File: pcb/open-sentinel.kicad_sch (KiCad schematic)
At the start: 0 parts

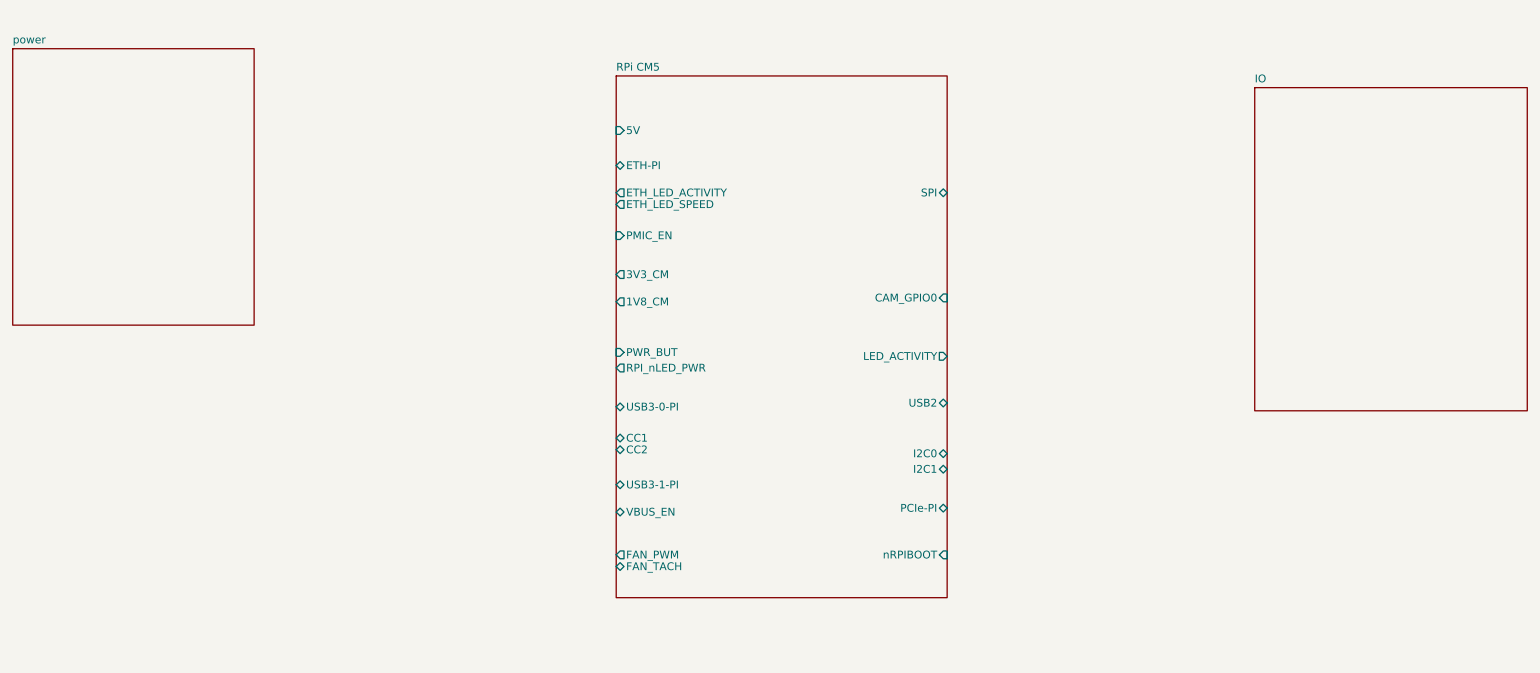
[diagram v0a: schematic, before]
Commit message: add HDMI and CSI pages
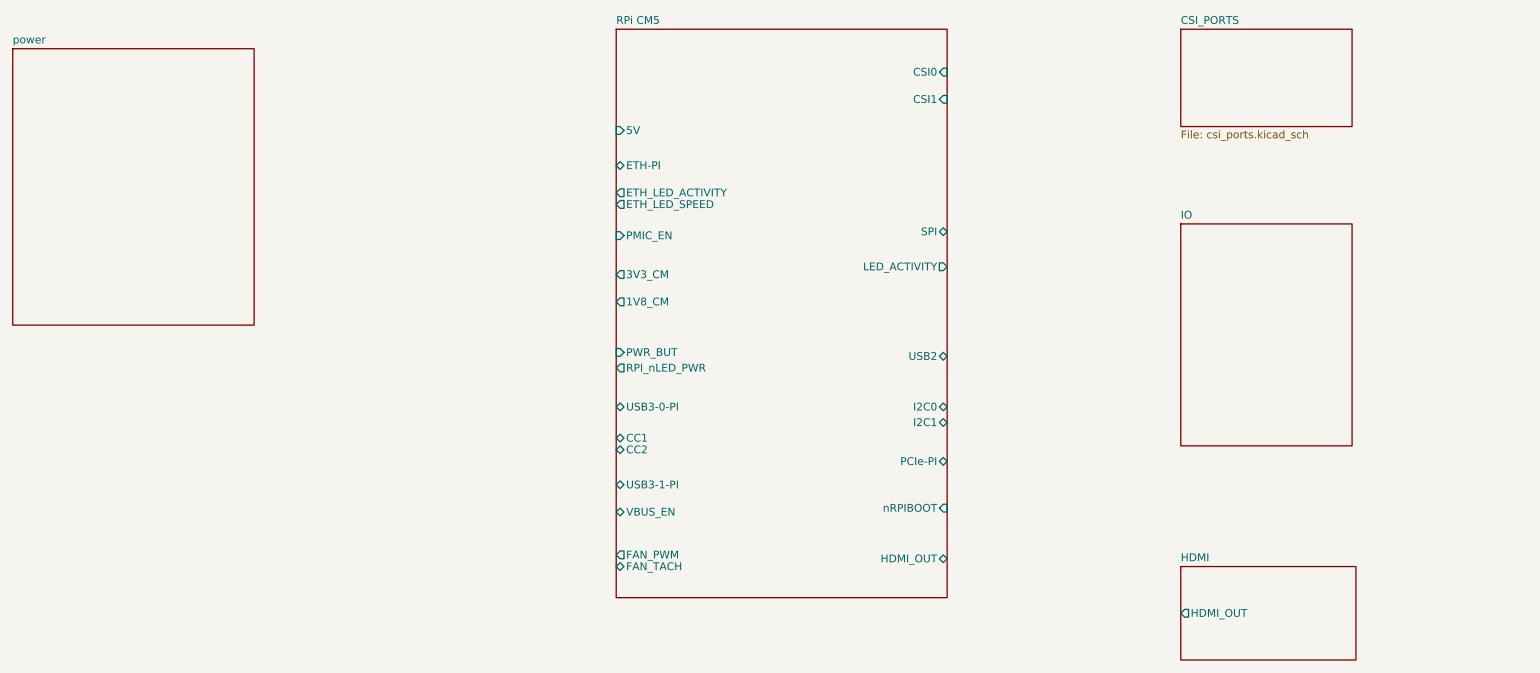
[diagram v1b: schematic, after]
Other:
- added sheet CSI_PORTS (csi_ports.kicad_sch)
- added sheet HDMI (hdmi.kicad_sch)
- sheet RPi CM5 ports: added CSI0, CSI1, HDMI_OUT; removed CAM_GPIO0
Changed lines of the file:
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@@
 	)
 	(sheet
-		(at 273.05 98.425)
-		(size 44.45 52.705)
+		(at 260.985 88.9)
+		(size 27.94 15.875)
+		(exclude_from_sim no)
+		(in_bom yes)
+		(on_board yes)
+		(dnp no)
+		(fields_autoplaced yes)
+		(stroke
+			(width 0.1524)
+			(type solid)
+			(color 132 0 0 1)
+		)
+		(fill
+			(color 255 255 194 1.0000)
+		)
+		(property "Sheetname" "CSI_PORTS"
+			(at 260.985 88.1884 0)
+			(effects
+				(font
+					(size 1.27 1.27)
+				)
+				(justify left bottom)
+			)
+		)
+		(property "Sheetfile" "csi_ports.kicad_sch"
+			(at 260.985 105.3596 0)
+			(effects
+				(font
+					(size 1.27 1.27)
+				)
+				(justify left top)
+			)
+		)
+		(instances
+			(project "open-sentinel"
+				(path "/b7d228cf-f9da-4203-b1ed-1128e1073415"
+					(page "6")
+				)
+			)
+		)
+	)
+	(sheet
+		(at 260.985 176.53)
+		(size 28.575 15.24)
 		(exclude_from_sim no)
 		(in_bom yes)
@@
 			(color 255 255 194 1.0000)
 		)
-		(property "Sheetname" "IO"
-			(at 273.05 97.7134 0)
+		(property "Sheetname" "HDMI"
+			(at 260.985 175.8184 0)
 			(effects
 				(font
@@
 			)
 		)
-		(property "Sheetfile" "io.kicad_sch"
-			(at 273.05 151.7146 0)
+		(property "Sheetfile" "hdmi.kicad_sch"
+			(at 260.985 192.3546 0)
 			(effects
 				(font
@@
 				(justify left top)
 				(hide yes)
+			)
+		)
+		(pin "HDMI_OUT" output
+			(at 260.985 184.15 180)
+			(effects
+				(font
+					(size 1.27 1.27)
+				)
+				(justify left)
 			)
 		)
@@
 			(project "open-sentinel"
 				(path "/b7d228cf-f9da-4203-b1ed-1128e1073415"
-					(page "4")
+					(page "5")
 				)
 			)
@@
 	)
 	(sheet
-		(at 168.91 96.52)
-		(size 53.975 85.09)
+		(at 260.985 120.65)
+		(size 27.94 36.195)
 		(exclude_from_sim no)
 		(in_bom yes)
@@
 			(color 255 255 194 1.0000)
 		)
+		(property "Sheetname" "IO"
+			(at 260.985 119.9384 0)
+			(effects
+				(font
+					(size 1.27 1.27)
+				)
+				(justify left bottom)
+			)
+		)
+		(property "Sheetfile" "io.kicad_sch"
+			(at 260.985 157.4296 0)
+			(effects
+				(font
+					(size 1.27 1.27)
+				)
+				(justify left top)
+				(hide yes)
+			)
+		)
+		(instances
+			(project "open-sentinel"
+				(path "/b7d228cf-f9da-4203-b1ed-1128e1073415"
+					(page "4")
+				)
+			)
+		)
+	)
+	(sheet
+		(at 168.91 88.9)
+		(size 53.975 92.71)
+		(exclude_from_sim no)
+		(in_bom yes)
+		(on_board yes)
+		(dnp no)
+		(fields_autoplaced yes)
+		(stroke
+			(width 0.1524)
+			(type solid)
+			(color 128 77 0 1)
+		)
+		(fill
+			(color 255 255 194 1.0000)
+		)
 		(property "Sheetname" "RPi CM5"
-			(at 168.91 95.8084 0)
+			(at 168.91 88.1884 0)
 			(effects
 				(font
@@
 		)
 		(pin "PCIe-PI" bidirectional
-			(at 222.885 167.005 0)
+			(at 222.885 159.385 0)
 			(effects
 				(font
@@
 		)
 		(pin "USB2" bidirectional
-			(at 222.885 149.86 0)
+			(at 222.885 142.24 0)
 			(effects
 				(font
@@
 			)
 		)
-		(pin "CAM_GPIO0" input
-			(at 222.885 132.715 0)
-			(effects
-				(font
-					(size 1.27 1.27)
-				)
-				(justify right)
-			)
-		)
 		(pin "CC1" bidirectional
 			(at 168.91 155.575 180)
@@
 		)
 		(pin "I2C0" bidirectional
-			(at 222.885 158.115 0)
+			(at 222.885 150.495 0)
 			(effects
 				(font
@@
 		)
 		(pin "I2C1" bidirectional
-			(at 222.885 160.655 0)
+			(at 222.885 153.035 0)
 			(effects
 				(font
@@
 		)
 		(pin "LED_ACTIVITY" output
-			(at 222.885 142.24 0)
+			(at 222.885 127.635 0)
 			(effects
 				(font
@@
 		)
 		(pin "nRPIBOOT" input
-			(at 222.885 174.625 0)
+			(at 222.885 167.005 0)
 			(effects
 				(font
@@
 		)
 		(pin "SPI" bidirectional
-			(at 222.885 115.57 0)
-			(effects
-				(font
+			(at 222.885 121.92 0)
+			(effects
+				(font
+					(size 1.27 1.27)
+				)
+				(justify right)
+			)
+		)
+		(pin "HDMI_OUT" bidirectional
+			(at 222.885 175.26 0)
+			(effects
+				(font
+					(size 1.27 1.27)
+				)
+				(justify right)
+			)
+		)
+		(pin "CSI0" input
+			(at 222.885 95.885 0)
+			(effects
+				(font
+					(size 1.27 1.27)
+				)
+				(justify right)
+			)
+		)
+		(pin "CSI1" input
+			(at 222.885 100.33 0)
+			(effects
+				(font

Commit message: finish M.2 slot schematic
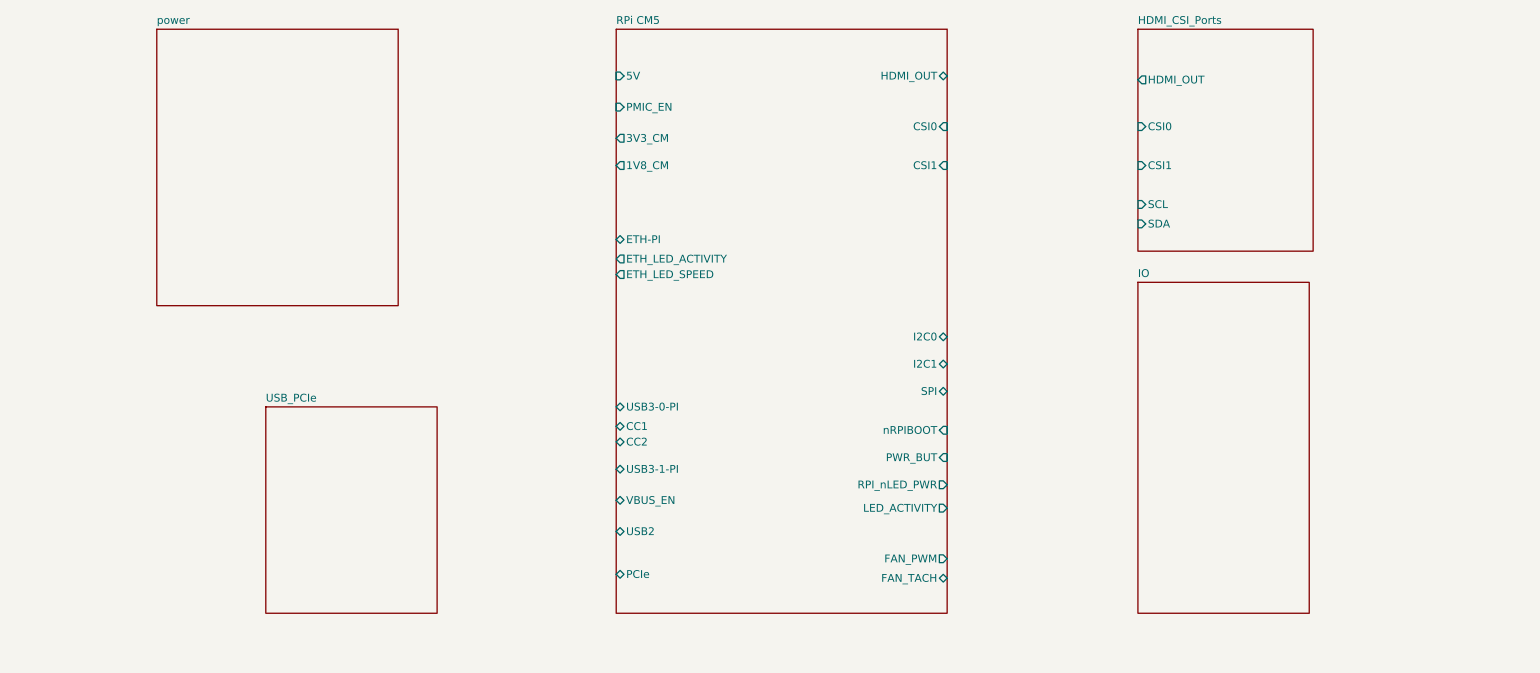
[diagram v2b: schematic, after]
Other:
- sheet HDMI renamed HDMI_CSI_Ports
- removed sheet CSI_PORTS
- added sheet USB_PCIe (usb_pcie.kicad_sch)
- sheet HDMI_CSI_Ports ports: added CSI0, CSI1, SCL, SDA; removed none
- sheet RPi CM5 ports: added PCIe; removed PCIe-PI
